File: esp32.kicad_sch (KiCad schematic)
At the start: 30 parts, among them J2 TC2030-IDC, J3 Conn_01x04, J4 USB_C_Receptacle_USB2.0, SW1 TL3330AF260QG, SW2 TL3330AF260QG, U7 RT9080-33GJ5, U8 ESP32-S3-WROOM-1, Y2 32.768kHz

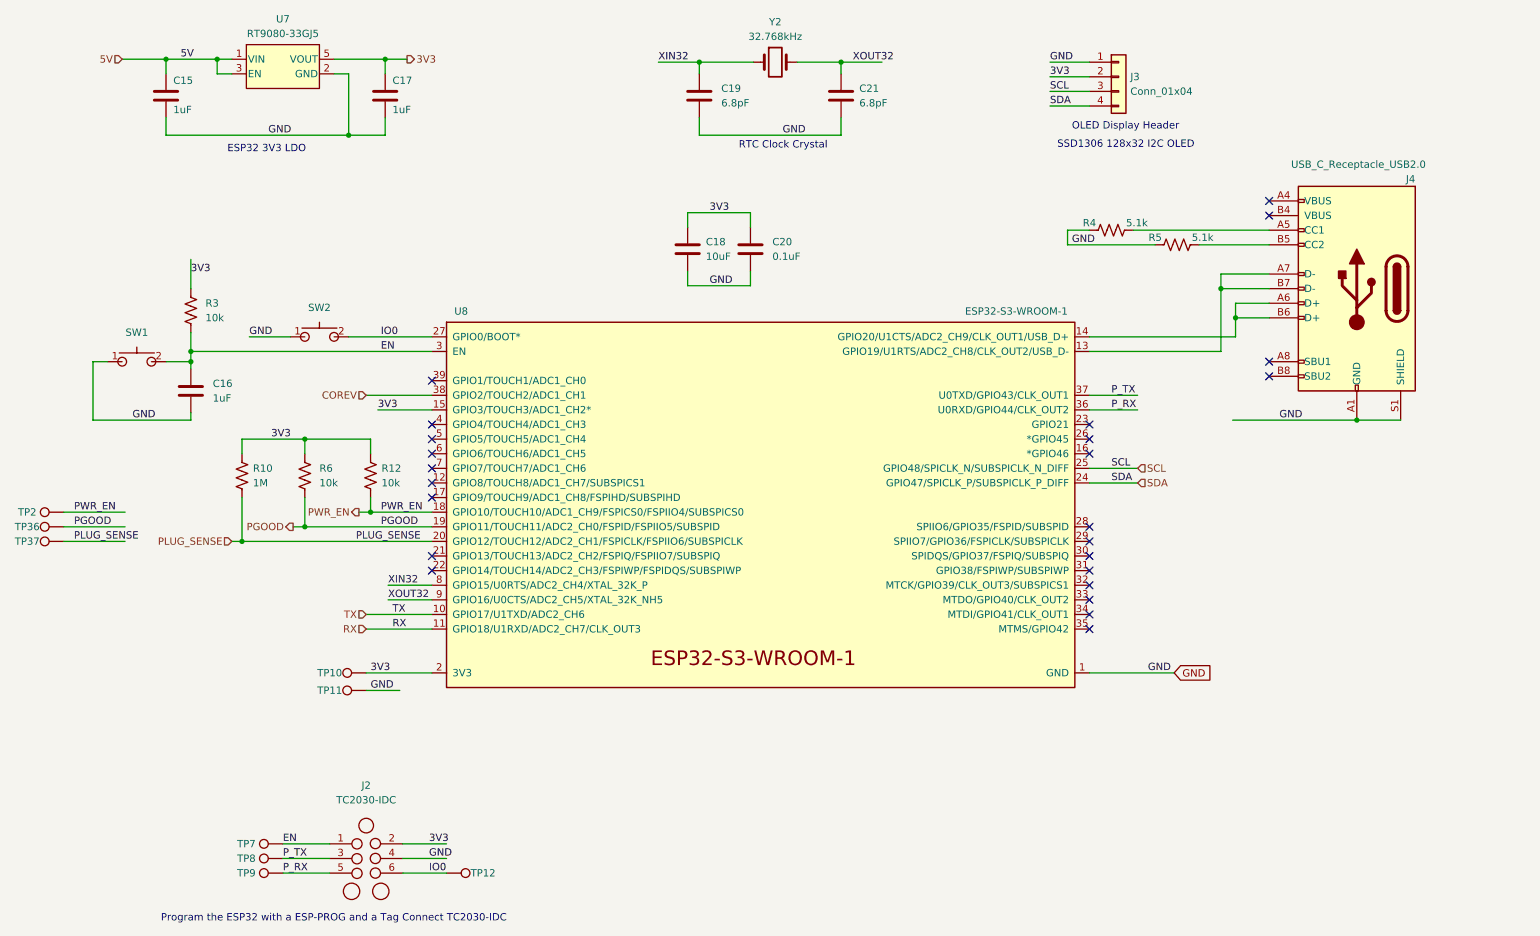
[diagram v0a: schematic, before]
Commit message: added stm32 crystal for #9
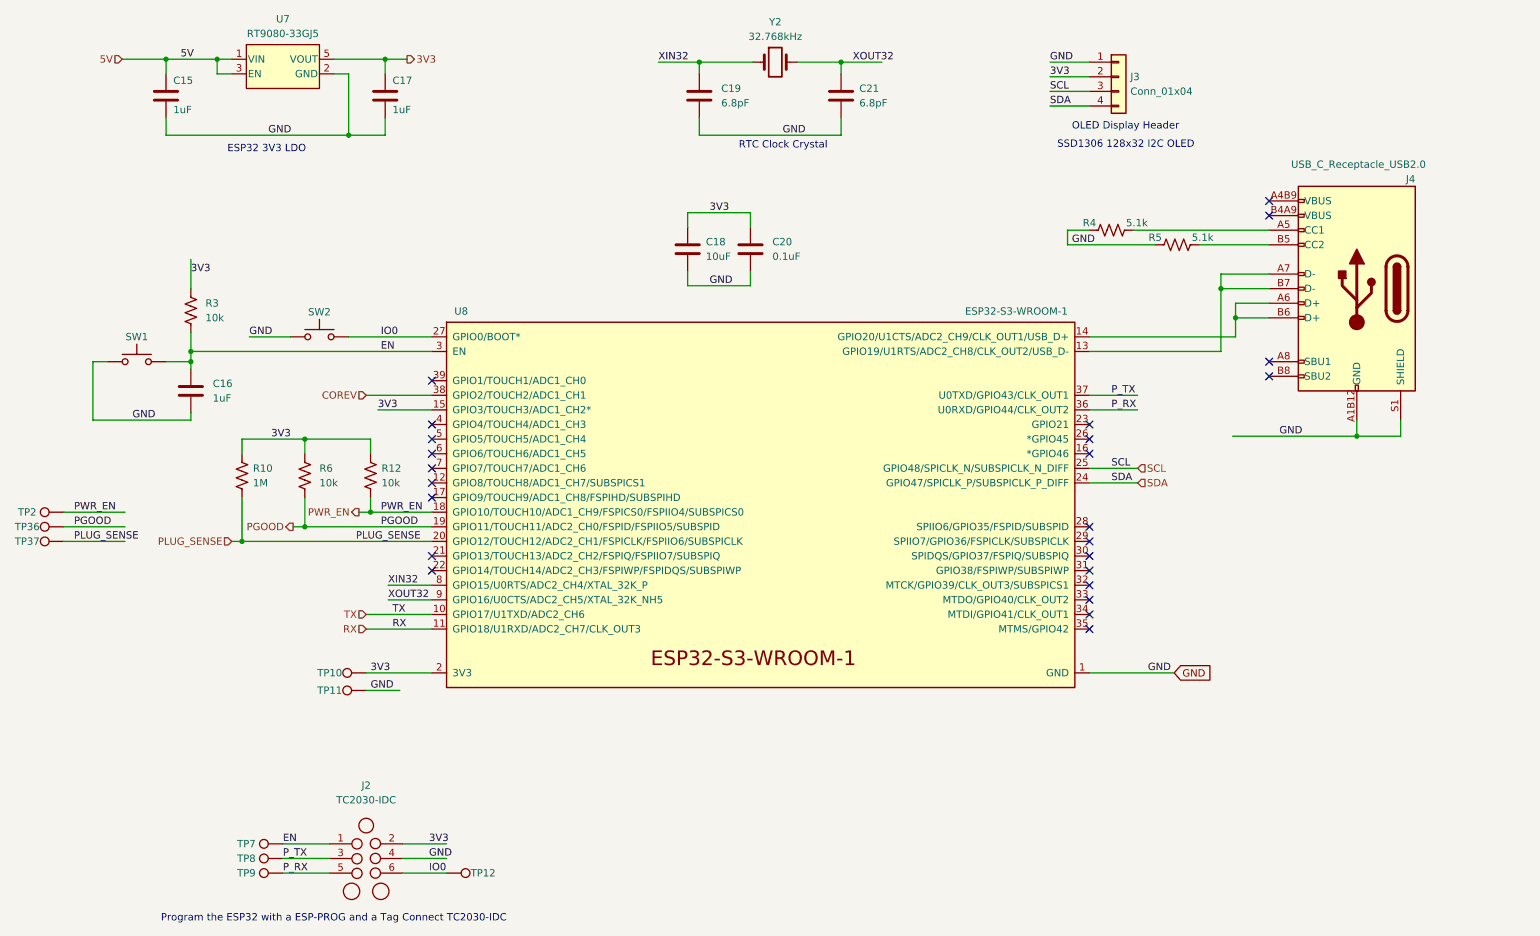
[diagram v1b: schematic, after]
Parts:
- SW1, SW2: symbol blockaxe:GT-TC029B-H025-L1N -> blockaxe:SW_Push
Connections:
- net GND: now also J4.A1B12 (GND), J4.B1A12 (GND); no longer J4.A1 (GND), J4.A12 (GND), J4.B1 (GND), J4.B12 (GND)
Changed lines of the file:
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@@
   (junction (at 40.132 27.432) (diameter 0) (color 0 0 0 0)
   )
+  (junction (at 247.142 92.964) (diameter 0) (color 0 0 0 0)
+  )
   (junction (at 53.34 111.252) (diameter 0) (color 0 0 0 0)
   )
@@
   )
   (junction (at 44.45 78.232) (diameter 0) (color 0 0 0 0)
-  )
-  (junction (at 247.142 90.17) (diameter 0) (color 0 0 0 0)
   )
   (junction (at 226.06 72.39) (diameter 0) (color 0 0 0 0)
@@
     (stroke (width 0) (type default))
   )
-  (wire (pts (xy 225.552 90.17) (xy 247.142 90.17))
-    (stroke (width 0) (type default))
-  )
-  (wire (pts (xy 247.142 90.17) (xy 254.762 90.17))
+  (wire (pts (xy 225.552 92.964) (xy 247.142 92.964))
+    (stroke (width 0) (type default))
+  )
+  (wire (pts (xy 247.142 92.964) (xy 254.762 92.964))
     (stroke (width 0) (type default))
   )
@@
     (stroke (width 0) (type default))
   )
+  (wire (pts (xy 247.142 92.964) (xy 247.142 90.17))
+    (stroke (width 0) (type default))
+  )
   (wire (pts (xy 22.352 108.712) (xy 33.02 108.712))
     (stroke (width 0) (type default))
@@
   )
   (wire (pts (xy 53.34 111.252) (xy 86.36 111.252))
+    (stroke (width 0) (type default))
+  )
+  (wire (pts (xy 254.762 92.964) (xy 254.762 90.17))
     (stroke (width 0) (type default))
   )
@@
     (effects (font (size 1.27 1.27)) (justify left bottom))
   )
-  (label "GND" (at 233.68 90.17 0) (fields_autoplaced)
+  (label "GND" (at 233.68 92.964 0) (fields_autoplaced)
     (effects (font (size 1.27 1.27)) (justify left bottom))
   )
@@
       (effects (font (size 1.27 1.27)) hide)
     )
-    (pin "A1")
-    (pin "A12")
-    (pin "A4")
+    (pin "A1B12")
+    (pin "B1A12")
+    (pin "A4B9")
     (pin "A5")
     (pin "A6")
     (pin "A7")
     (pin "A8")
-    (pin "A9")
-    (pin "B1")
-    (pin "B12")
-    (pin "B4")
+    (pin "B4A9")
     (pin "B5")
     (pin "B6")
     (pin "B7")
     (pin "B8")
-    (pin "B9")
     (pin "S1")
     (instances
@@
     )
   )
-  (symbol (lib_id "blockaxe:GT-TC029B-H025-L1N") (at 35.052 80.01 0) (unit 1)
-    (in_bom yes) (on_board yes) (dnp no) (fields_autoplaced)
-    (property "Reference" "SW1" (at 35.052 74.93 0)
+  (symbol (lib_id "blockaxe:SW_Push") (at 35.052 80.01 0) (unit 1)
+    (in_bom yes) (on_board yes) (dnp no)
+    (property "Reference" "SW1" (at 35.052 75.692 0)
       (effects (font (size 1.27 1.27)))
     )
@@
       (effects (font (size 1.27 1.27)) hide)
     )
-    (property "Footprint" "blockaxe:SW_TL3330_EWI" (at 35.052 87.63 0)
-      (effects (font (size 1.27 1.27)) hide)
-    )
-    (property "Datasheet" "https://api.pim.na.industrial.panasonic.com/file_stream/main/fileversion/245500" (at 35.052 90.17 0)
-      (effects (font (size 1.27 1.27)) hide)
-    )
-    (property "DK" "EG4389CT-ND" (at 35.052 80.01 0)
-      (effects (font (size 1.27 1.27)) hide)
-    )
-    (property "PARTNO" "TL3330AF260QG" (at 35.052 80.01 0)
-      (effects (font (size 1.27 1.27)) hide)
-    )
-    (pin "1")
-    (pin "2")
+    (property "Footprint" "blockaxe:SW_TL3330_EWI" (at 36.322 68.58 0)
+      (effects (font (size 1.27 1.27)) hide)
+    )
+    (property "Datasheet" "https://api.pim.na.industrial.panasonic.com/file_stream/main/fileversion/245500" (at 36.322 68.58 0)
+      (effects (font (size 1.27 1.27)) hide)
+    )
+    (property "DK" "EG4389CT-ND" (at 35.052 74.93 0)
+      (effects (font (size 1.27 1.27)) hide)
+    )
+    (property "PARTNO" "TL3330AF260QG" (at 35.052 73.66 0)
+      (effects (font (size 1.27 1.27)) hide)
+    )
+    (pin "1")
+    (pin "2")
+    (pin "4")
+    (pin "3")
     (instances
       (project "blockaxe1"
@@
     )
   )
-  (symbol (lib_id "blockaxe:GT-TC029B-H025-L1N") (at 66.802 75.692 0) (unit 1)
-    (in_bom yes) (on_board yes) (dnp no) (fields_autoplaced)
-    (property "Reference" "SW2" (at 66.802 70.612 0)
+  (symbol (lib_id "blockaxe:SW_Push") (at 66.802 75.692 0) (unit 1)
+    (in_bom yes) (on_board yes) (dnp no)
+    (property "Reference" "SW2" (at 66.802 71.374 0)
       (effects (font (size 1.27 1.27)))
     )
@@
       (effects (font (size 1.27 1.27)) hide)
     )
-    (property "Footprint" "blockaxe:SW_TL3330_EWI" (at 66.802 83.312 0)
-      (effects (font (size 1.27 1.27)) hide)
-    )
-    (property "Datasheet" "https://sten-eswitch-13110800-production.s3.amazonaws.com/system/asset/product_line/data_sheet/163/TL3330.pdf" (at 66.802 85.852 0)
-      (effects (font (size 1.27 1.27)) hide)
-    )
-    (property "DK" "EG4389CT-ND" (at 66.802 75.692 0)
-      (effects (font (size 1.27 1.27)) hide)
-    )
-    (property "PARTNO" "TL3330AF260QG" (at 66.802 75.692 0)
-      (effects (font (size 1.27 1.27)) hide)
-    )
-    (pin "1")
-    (pin "2")
-    (instances
-      (project "blockaxe1"
+    (property "Footprint" "blockaxe:SW_TL3330_EWI" (at 68.072 64.262 0)
+      (effects (font (size 1.27 1.27)) hide)
+    )
+    (property "Datasheet" "https://api.pim.na.industrial.panasonic.com/file_stream/main/fileversion/245500" (at 68.072 64.262 0)
+      (effects (font (size 1.27 1.27)) hide)
+    )
+    (property "DK" "EG4389CT-ND" (at 66.802 70.612 0)
+      (effects (font (size 1.27 1.27)) hide)
+    )
+    (property "PARTNO" "TL3330AF260QG" (at 66.802 69.342 0)
+      (effects (font (size 1.27 1.27)) hide)
+    )
+    (pin "1")
+    (pin "2")
+    (pin "4")
+    (pin "3")
+    (instances
+      (project "blockaxe1"

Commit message: generated gerbers, updated BOM C18 error
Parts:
- C18: DK 399-C0805C106K8PAC7800DKR-ND -> 399-C0805C106K8PAC7800CT-ND
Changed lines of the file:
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@@
       (effects (font (size 1.27 1.27)) hide)
     )
-    (property "DK" "399-C0805C106K8PAC7800DKR-ND" (at 130.81 60.452 0)
+    (property "DK" "399-C0805C106K8PAC7800CT-ND" (at 130.81 60.452 0)
       (effects (font (size 1.27 1.27)) hide)
     )

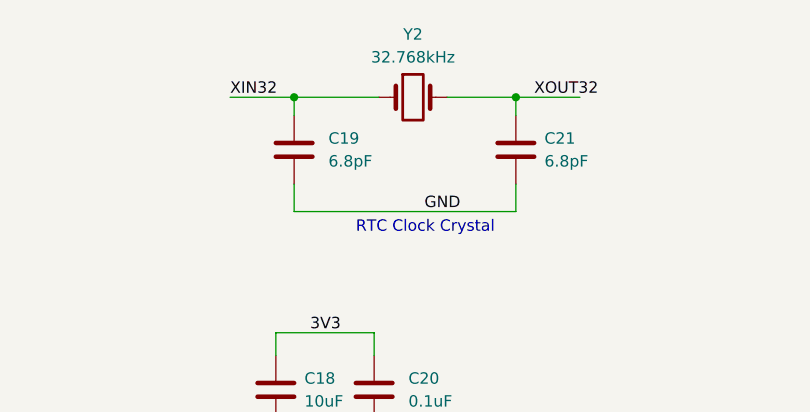
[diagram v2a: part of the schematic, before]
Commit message: update to KiCad8, DNP 32kHz crystal
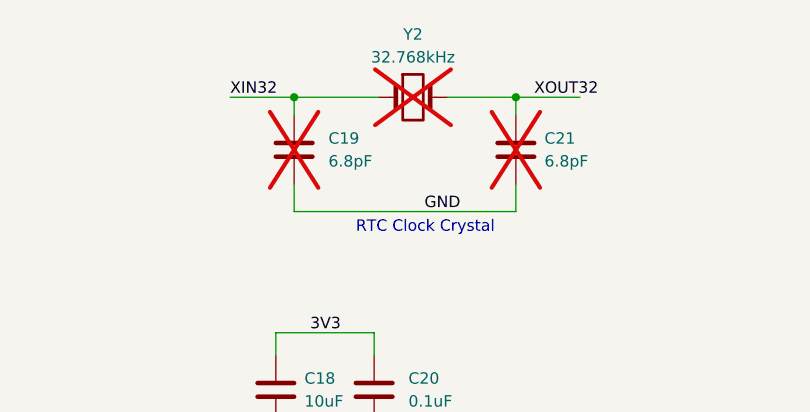
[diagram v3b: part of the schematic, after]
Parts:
- C19, C21, Y2: now not fitted; now left out of the parts list
